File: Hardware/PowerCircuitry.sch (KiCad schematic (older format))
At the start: 25 parts

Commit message: Added master switch etc
I don't like MOSFETs
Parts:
- removed Battery: 3.6V, symbol Device:Battery
- removed Q? (x2): 2N7000, Package_TO_SOT_THT:TO-92_Inline, symbol Transistor_FET:2N7000
- added Battery: Conn_01x02_Male, symbol Connector:Conn_01x02_Male
- added Q? (x2): MMBT3904, Package_TO_SOT_SMD:SOT-23, symbol Transistor_BJT:MMBT3904
- added SW?: SW_Push, symbol Switch:SW_Push
- C2.2: footprint (none) -> Capacitor_SMD:C_0603_1608Metric
- RSense1, RSense2: value 30mOhms -> 30m
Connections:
- wire segments 68 -> 69
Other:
- moved on the sheet: 12VBoostConverter, 3V3Regulator, 6VBoostConverter, C1.1, C1.2, C1.3, C1.4, C2.1, C2.2, C2.3, C2.4, C2.5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

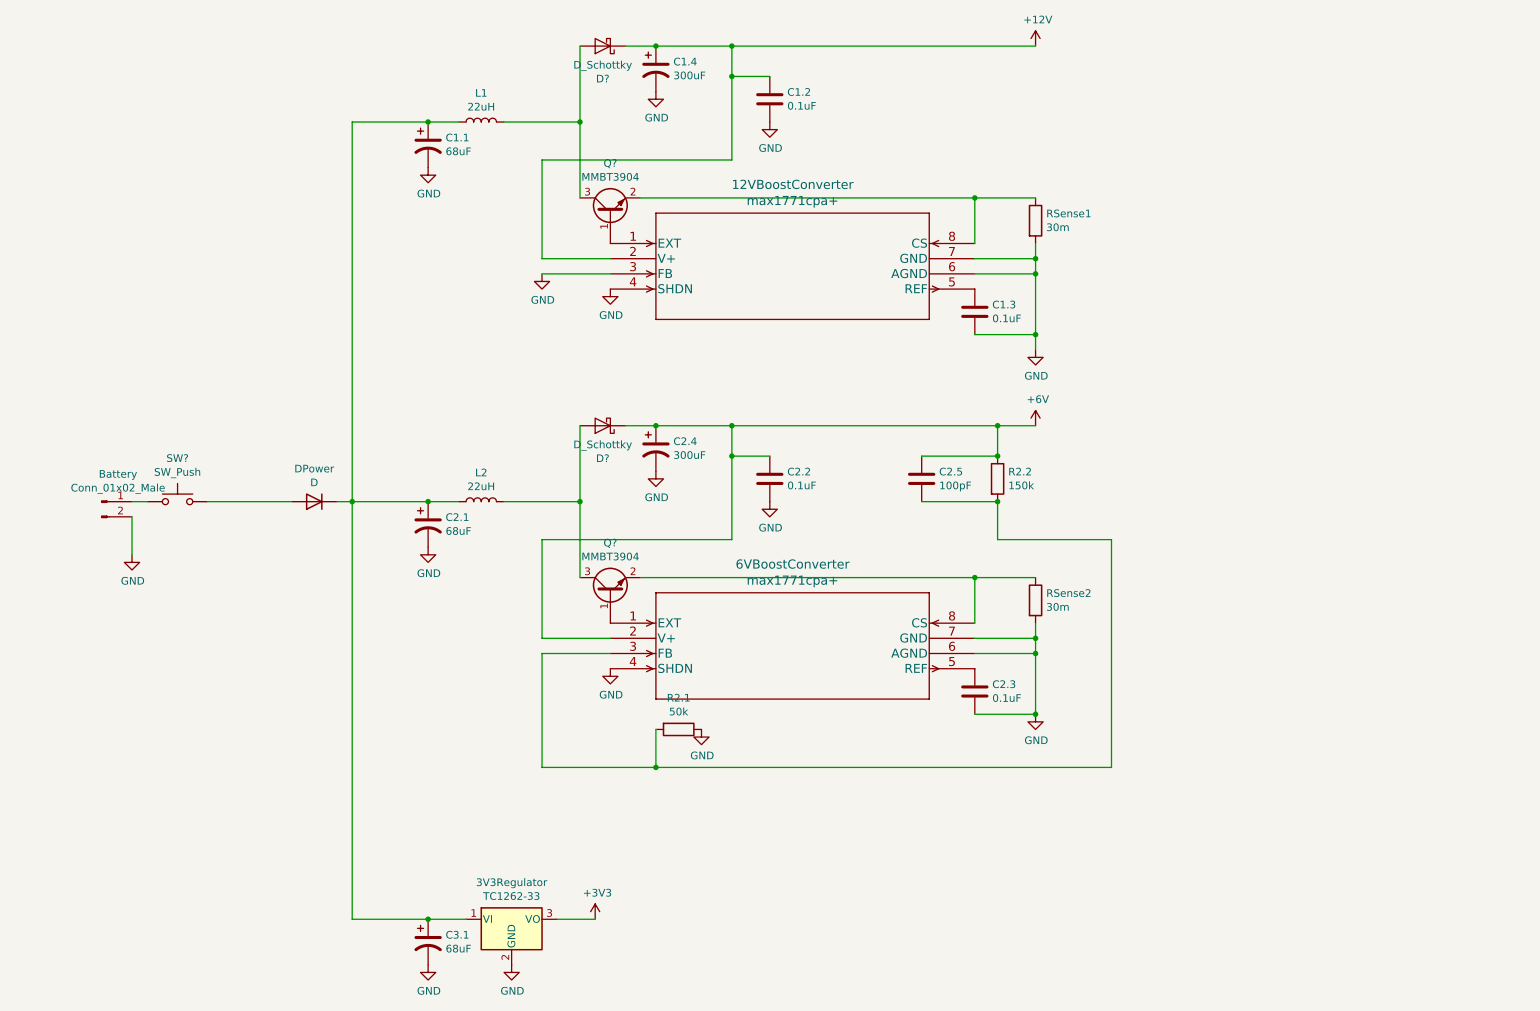
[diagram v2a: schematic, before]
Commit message: Fixed some of the ERC errors
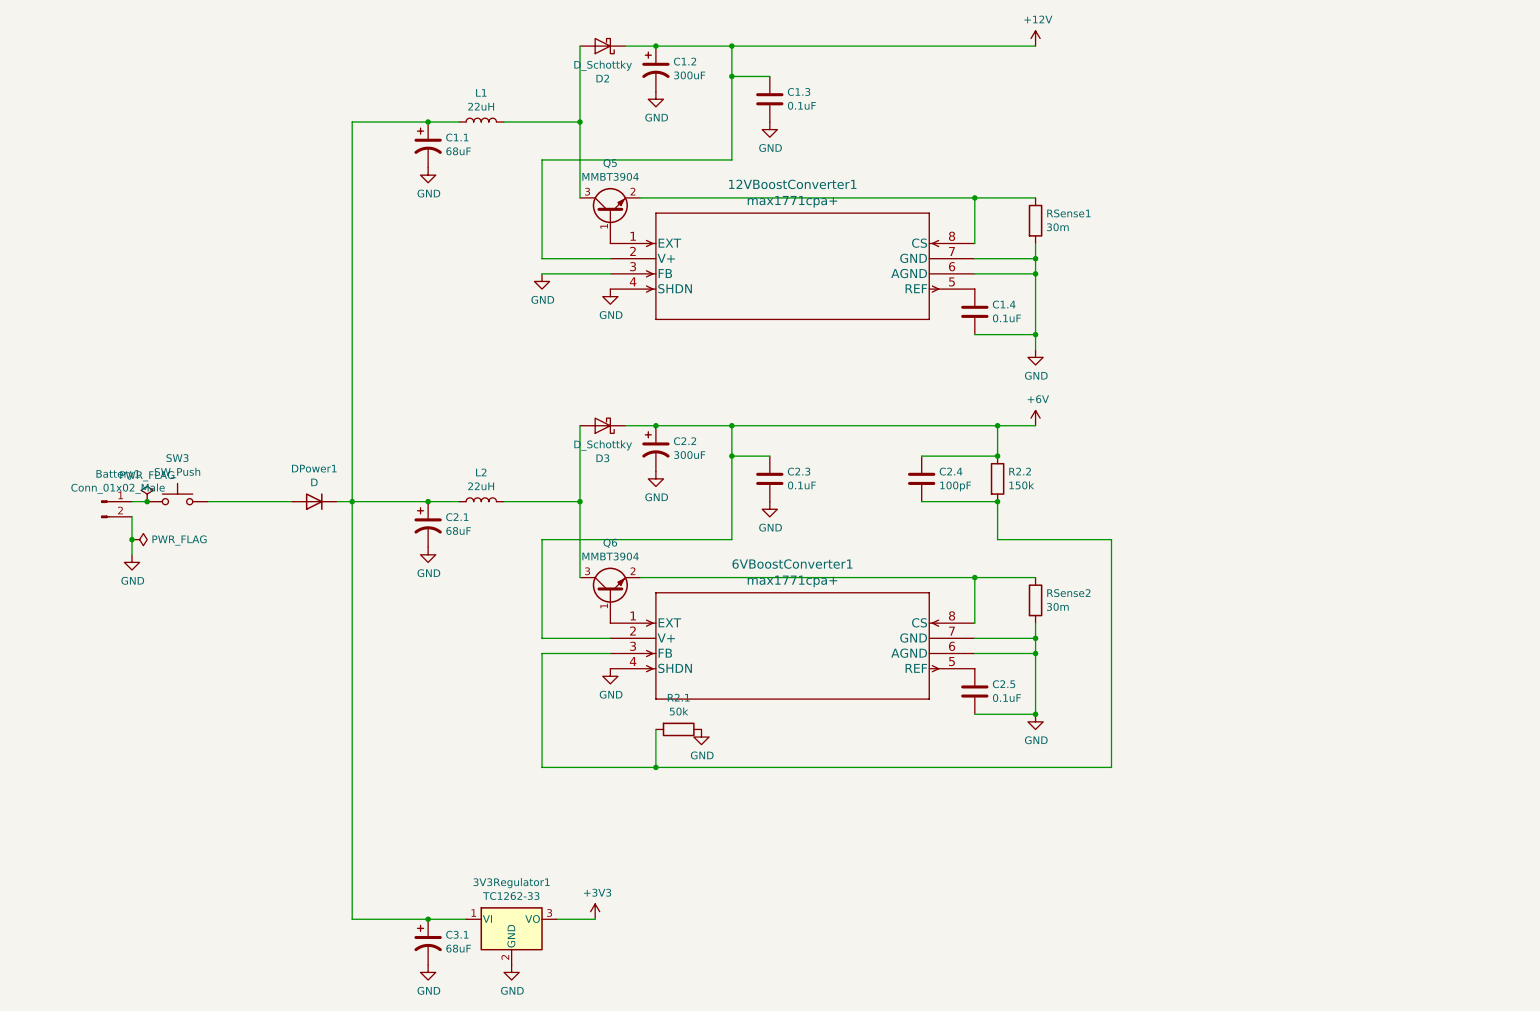
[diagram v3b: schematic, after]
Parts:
- gave numbers to parts that had none: 5
- renumbered 12VBoostConverter to 12VBoostConverter1, 3V3Regulator to 3V3Regulator1, 6VBoostConverter to 6VBoostConverter1, Battery to Battery1, C1.4 to C1.2, C1.2 to C1.3, C1.3 to C1.4, C2.4 to C2.2, C2.2 to C2.3, C2.5 to C2.4, C2.3 to C2.5, DPower to DPower1

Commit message: Created PCB file and laid out components
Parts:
- removed SW3: SW_Push, symbol Switch:SW_Push
- added H1, H2, H3, H4: MountingHole_Pad, MountingHole:MountingHole_3.5mm_Pad_TopBottom, symbol Mechanical:MountingHole_Pad
- added SW3: SW_SPST, Button_Switch_SMD:SW_DIP_SPSTx01_Slide_6.7x4.1mm_W6.73mm_P2.54mm_LowProfile_JPin, symbol Switch:SW_SPST
- 12VBoostConverter1, 6VBoostConverter1: footprint 21-0043D_8_MXM -> footprints:max1771cpa&plus_
- 3V3Regulator1: footprint (none) -> Package_TO_SOT_SMD:SOT-223-3_TabPin2
- Battery1: footprint (none) -> Connector_JST:JST_EH_B2B-EH-A_1x02_P2.50mm_Vertical
- C1.1, C1.2, C1.3, C1.4, C2.1, C2.2, C2.4, C2.5, C3.1: footprint (none) -> Capacitor_SMD:C_0603_1608Metric
- D2, D3, DPower1: footprint (none) -> Diode_SMD:D_0603_1608Metric
- L1, L2: footprint (none) -> Inductor_SMD:L_0603_1608Metric
- R2.1, R2.2, RSense1, RSense2: footprint (none) -> Resistor_SMD:R_0603_1608Metric
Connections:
- net GND: now also H1.1, H2.1, H3.1, H4.1
- net at Battery1.1 (Pin_1): now also SW3.1 (A)
- net at DPower1.2 (A): now also SW3.2 (B)
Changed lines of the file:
@@
 F 0 "3V3Regulator1" H 3500 6742 50  0000 C CNN
 F 1 "TC1262-33" H 3500 6651 50  0000 C CNN
-F 2 "" H 3500 6725 50  0001 C CIN
+F 2 "Package_TO_SOT_SMD:SOT-223-3_TabPin2" H 3500 6725 50  0001 C CIN
 F 3 "http://ww1.microchip.com/downloads/en/DeviceDoc/21373C.pdf" H 3500 6200 50  0001 C CNN
 	1    3500 6500
@@
 F 0 "12VBoostConverter1" H 5350 2437 60  0000 C CNN
 F 1 "max1771cpa+" H 5350 2331 60  0000 C CNN
-F 2 "21-0043D_8_MXM" H 5350 2290 60  0001 C CNN
+F 2 "footprints:max1771cpa&plus_" H 5350 2290 60  0001 C CNN
 F 3 "" H 4150 2050 60  0000 C CNN
 	1    4150 2050
@@
 F 0 "L1" V 3490 1250 50  0000 C CNN
 F 1 "22uH" V 3399 1250 50  0000 C CNN
-F 2 "" H 3300 1250 50  0001 C CNN
+F 2 "Inductor_SMD:L_0603_1608Metric" H 3300 1250 50  0001 C CNN
 F 3 "~" H 3300 1250 50  0001 C CNN
 	1    3300 1250
@@
 F 0 "D2" H 4100 966 50  0000 C CNN
 F 1 "D_Schottky" H 4100 875 50  0000 C CNN
-F 2 "" H 4100 750 50  0001 C CNN
+F 2 "Diode_SMD:D_0603_1608Metric" H 4100 750 50  0001 C CNN
 F 3 "~" H 4100 750 50  0001 C CNN
 	1    4100 750
@@
 F 0 "C1.1" H 3065 1446 50  0000 L CNN
 F 1 "68uF" H 3065 1355 50  0000 L CNN
-F 2 "" H 2950 1400 50  0001 C CNN
+F 2 "Capacitor_SMD:C_0603_1608Metric" H 2950 1400 50  0001 C CNN
 F 3 "~" H 2950 1400 50  0001 C CNN
 	1    2950 1400
@@
 F 0 "C1.2" H 4565 946 50  0000 L CNN
 F 1 "300uF" H 4565 855 50  0000 L CNN
-F 2 "" H 4450 900 50  0001 C CNN
+F 2 "Capacitor_SMD:C_0603_1608Metric" H 4450 900 50  0001 C CNN
 F 3 "~" H 4450 900 50  0001 C CNN
 	1    4450 900
@@
 F 0 "C1.3" H 5315 1146 50  0000 L CNN
 F 1 "0.1uF" H 5315 1055 50  0000 L CNN
-F 2 "" H 5238 950 50  0001 C CNN
+F 2 "Capacitor_SMD:C_0603_1608Metric" H 5238 950 50  0001 C CNN
 F 3 "~" H 5200 1100 50  0001 C CNN
 	1    5200 1100
@@
 F 0 "RSense1" H 7020 1946 50  0000 L CNN
 F 1 "30m" H 7020 1855 50  0000 L CNN
-F 2 "" V 6880 1900 50  0001 C CNN
+F 2 "Resistor_SMD:R_0603_1608Metric" V 6880 1900 50  0001 C CNN
 F 3 "~" H 6950 1900 50  0001 C CNN
 	1    6950 1900
@@
 F 0 "C2.1" H 3065 3946 50  0000 L CNN
 F 1 "68uF" H 3065 3855 50  0000 L CNN
-F 2 "" H 2950 3900 50  0001 C CNN
+F 2 "Capacitor_SMD:C_0603_1608Metric" H 2950 3900 50  0001 C CNN
 F 3 "~" H 2950 3900 50  0001 C CNN
 	1    2950 3900
@@
 F 0 "L2" V 3490 3750 50  0000 C CNN
 F 1 "22uH" V 3399 3750 50  0000 C CNN
-F 2 "" H 3300 3750 50  0001 C CNN
+F 2 "Inductor_SMD:L_0603_1608Metric" H 3300 3750 50  0001 C CNN
 F 3 "~" H 3300 3750 50  0001 C CNN
 	1    3300 3750
@@
 F 0 "D3" H 4100 3466 50  0000 C CNN
 F 1 "D_Schottky" H 4100 3375 50  0000 C CNN
-F 2 "" H 4100 3250 50  0001 C CNN
+F 2 "Diode_SMD:D_0603_1608Metric" H 4100 3250 50  0001 C CNN
 F 3 "~" H 4100 3250 50  0001 C CNN
 	1    4100 3250
@@
 F 0 "C2.2" H 4565 3446 50  0000 L CNN
 F 1 "300uF" H 4565 3355 50  0000 L CNN
-F 2 "" H 4450 3400 50  0001 C CNN
+F 2 "Capacitor_SMD:C_0603_1608Metric" H 4450 3400 50  0001 C CNN
 F 3 "~" H 4450 3400 50  0001 C CNN
 	1    4450 3400
@@
 F 0 "R2.2" H 6770 3646 50  0000 L CNN
 F 1 "150k" H 6770 3555 50  0000 L CNN
-F 2 "" V 6630 3600 50  0001 C CNN
+F 2 "Resistor_SMD:R_0603_1608Metric" V 6630 3600 50  0001 C CNN
 F 3 "~" H 6700 3600 50  0001 C CNN
 	1    6700 3600
@@
 F 0 "C2.4" H 6315 3646 50  0000 L CNN
 F 1 "100pF" H 6315 3555 50  0000 L CNN
-F 2 "" H 6238 3450 50  0001 C CNN
+F 2 "Capacitor_SMD:C_0603_1608Metric" H 6238 3450 50  0001 C CNN
 F 3 "~" H 6200 3600 50  0001 C CNN
 	1    6200 3600
@@
 F 0 "RSense2" H 7020 4446 50  0000 L CNN
 F 1 "30m" H 7020 4355 50  0000 L CNN
-F 2 "" V 6880 4400 50  0001 C CNN
+F 2 "Resistor_SMD:R_0603_1608Metric" V 6880 4400 50  0001 C CNN
 F 3 "~" H 6950 4400 50  0001 C CNN
 	1    6950 4400
@@
 F 0 "R2.1" V 4393 5250 50  0000 C CNN
 F 1 "50k" V 4484 5250 50  0000 C CNN
-F 2 "" V 4530 5250 50  0001 C CNN
+F 2 "Resistor_SMD:R_0603_1608Metric" V 4530 5250 50  0001 C CNN
 F 3 "~" H 4600 5250 50  0001 C CNN
 	1    4600 5250
@@
 F 0 "C1.4" H 6665 2546 50  0000 L CNN
 F 1 "0.1uF" H 6665 2455 50  0000 L CNN
-F 2 "" H 6588 2350 50  0001 C CNN
+F 2 "Capacitor_SMD:C_0603_1608Metric" H 6588 2350 50  0001 C CNN
 F 3 "~" H 6550 2500 50  0001 C CNN
 	1    6550 2500
@@
 F 0 "C2.5" H 6665 5046 50  0000 L CNN
 F 1 "0.1uF" H 6665 4955 50  0000 L CNN
-F 2 "" H 6588 4850 50  0001 C CNN
+F 2 "Capacitor_SMD:C_0603_1608Metric" H 6588 4850 50  0001 C CNN
 F 3 "~" H 6550 5000 50  0001 C CNN
 	1    6550 5000
@@
 F 0 "C3.1" H 3065 6696 50  0000 L CNN
 F 1 "68uF" H 3065 6605 50  0000 L CNN
-F 2 "" H 2950 6650 50  0001 C CNN
+F 2 "Capacitor_SMD:C_0603_1608Metric" H 2950 6650 50  0001 C CNN
 F 3 "~" H 2950 6650 50  0001 C CNN
 	1    2950 6650
@@
 Connection ~ 2950 6500
 $Comp
-L Switch:SW_Push SW3
-U 1 1 607B163F
-P 1300 3750
-F 0 "SW3" H 1300 4035 50  0000 C CNN
-F 1 "SW_Push" H 1300 3944 50  0000 C CNN
-F 2 "" H 1300 3950 50  0001 C CNN
-F 3 "~" H 1300 3950 50  0001 C CNN
-	1    1300 3750
-	1    0    0    -1
-$EndComp
-$Comp
 L Device:D DPower1
 U 1 1 607B8542
@@
 F 0 "DPower1" H 2200 3534 50  0000 C CNN
 F 1 "D" H 2200 3625 50  0000 C CNN
-F 2 "" H 2200 3750 50  0001 C CNN
+F 2 "Diode_SMD:D_0603_1608Metric" H 2200 3750 50  0001 C CNN
 F 3 "~" H 2200 3750 50  0001 C CNN
 	1    2200 3750
@@
 F 0 "Battery1" H 908 3931 50  0000 C CNN
 F 1 "Conn_01x02_Male" H 908 3840 50  0000 C CNN
-F 2 "" H 800 3750 50  0001 C CNN
+F 2 "Connector_JST:JST_EH_B2B-EH-A_1x02_P2.50mm_Vertical" H 800 3750 50  0001 C CNN
 F 3 "~" H 800 3750 50  0001 C CNN
 	1    800  3750
@@
 F 0 "6VBoostConverter1" H 5350 4937 60  0000 C CNN
 F 1 "max1771cpa+" H 5350 4831 60  0000 C CNN
-F 2 "21-0043D_8_MXM" H 5350 4790 60  0001 C CNN
+F 2 "footprints:max1771cpa&plus_" H 5350 4790 60  0001 C CNN
 F 3 "" H 4150 4550 60  0000 C CNN
 	1    4150 4550
@@
 Wire Wire Line
 	1500 3750 2050 3750
+Wire Wire Line
+	2450 1250 2450 3750
+$Comp
+L Switch:SW_SPST SW3
+U 1 1 608DCB23
+P 1300 3750
+F 0 "SW3" H 1300 3985 50  0000 C CNN
+F 1 "SW_SPST" H 1300 3894 50  0000 C CNN
+F 2 "Button_Switch_SMD:SW_DIP_SPSTx01_Slide_6.7x4.1mm_W6.73mm_P2.54mm_LowProfile_JPin" H 1300 3750 50  0001 C CNN
+F 3 "~" H 1300 3750 50  0001 C CNN
+	1    1300 3750
+	1    0    0    -1
+$EndComp
 Connection ~ 1100 3750
-Wire Wire Line
-	2450 1250 2450 3750
+$Comp
+L Mechanical:MountingHole_Pad H1
+U 1 1 6090A199
+P 9100 1450
+F 0 "H1" V 9054 1600 50  0000 L CNN
+F 1 "MountingHole_Pad" V 9145 1600 50  0000 L CNN
+F 2 "MountingHole:MountingHole_3.5mm_Pad_TopBottom" H 9100 1450 50  0001 C CNN
+F 3 "~" H 9100 1450 50  0001 C CNN
+	1    9100 1450
+	0    1    1    0
+$EndComp
+$Comp
+L Mechanical:MountingHole_Pad H2
+U 1 1 6090BABB
+P 9100 1650
+F 0 "H2" V 9054 1800 50  0000 L CNN
+F 1 "MountingHole_Pad" V 9145 1800 50  0000 L CNN
+F 2 "MountingHole:MountingHole_3.5mm_Pad_TopBottom" H 9100 1650 50  0001 C CNN
+F 3 "~" H 9100 1650 50  0001 C CNN
+	1    9100 1650
+	0    1    1    0
+$EndComp
+$Comp
+L Mechanical:MountingHole_Pad H3
+U 1 1 6090BF65
+P 9100 1850
+F 0 "H3" V 9054 2000 50  0000 L CNN
+F 1 "MountingHole_Pad" V 9145 2000 50  0000 L CNN
+F 2 "MountingHole:MountingHole_3.5mm_Pad_TopBottom" H 9100 1850 50  0001 C CNN
+F 3 "~" H 9100 1850 50  0001 C CNN
+	1    9100 1850
+	0    1    1    0
+$EndComp
+$Comp
+L Mechanical:MountingHole_Pad H4
+U 1 1 6090BF6B
+P 9100 2050
+F 0 "H4" V 9054 2200 50  0000 L CNN
+F 1 "MountingHole_Pad" V 9145 2200 50  0000 L CNN
+F 2 "MountingHole:MountingHole_3.5mm_Pad_TopBottom" H 9100 2050 50  0001 C CNN
+F 3 "~" H 9100 2050 50  0001 C CNN
+	1    9100 2050
+	0    1    1    0
+$EndComp
+Wire Wire Line
+	9000 1450 9000 1650
+Connection ~ 9000 1650
+Wire Wire Line
+	9000 1650 9000 1750
+Connection ~ 9000 1850
+Wire Wire Line
+	9000 1850 9000 2050
+$Comp
+L power:GND #PWR053
+U 1 1 6090F428
+P 9000 1750
+F 0 "#PWR053" H 9000 1500 50  0001 C CNN
+F 1 "GND" V 9005 1622 50  0000 R CNN
+F 2 "" H 9000 1750 50  0001 C CNN
+F 3 "" H 9000 1750 50  0001 C CNN
+	1    9000 1750
+	0    1    1    0
+$EndComp
+Connection ~ 9000 1750
+Wire Wire Line
+	9000 1750 9000 1850
 $EndSCHEMATC

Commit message: Final changes for this first draft
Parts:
- added J4, J5: Conn_01x02_Male, Connector_PinHeader_2.54mm:PinHeader_2x01_P2.54mm_Vertical, symbol Connector:Conn_01x02_Male
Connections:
- net +12V: now also J4.2 (Pin_2)
- net +6V: now also J5.2 (Pin_2)
- net GND: now also J4.1 (Pin_1), J5.1 (Pin_1)
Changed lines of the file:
@@
 Wire Wire Line
 	9000 1750 9000 1850
+$Comp
+L Connector:Conn_01x02_Male J4
+U 1 1 609DE2A3
+P 9400 3000
+F 0 "J4" H 9372 2882 50  0000 R CNN
+F 1 "Conn_01x02_Male" H 9372 2973 50  0000 R CNN
+F 2 "Connector_PinHeader_2.54mm:PinHeader_2x01_P2.54mm_Vertical" H 9400 3000 50  0001 C CNN
+F 3 "~" H 9400 3000 50  0001 C CNN
+	1    9400 3000
+	-1   0    0    1
+$EndComp
+Wire Wire Line
+	9200 2900 9100 2900
+Wire Wire Line
+	9200 3000 9100 3000
+Wire Wire Line
+	9100 3000 9100 3100
+Wire Wire Line
+	9100 2900 9100 2800
+$Comp
+L power:+12V #PWR054
+U 1 1 609E333D
+P 9100 2800
+F 0 "#PWR054" H 9100 2650 50  0001 C CNN
+F 1 "+12V" H 9115 2973 50  0000 C CNN
+F 2 "" H 9100 2800 50  0001 C CNN
+F 3 "" H 9100 2800 50  0001 C CNN
+	1    9100 2800
+	1    0    0    -1
+$EndComp
+$Comp
+L power:GND #PWR055
+U 1 1 609E5451
+P 9100 3100
+F 0 "#PWR055" H 9100 2850 50  0001 C CNN
+F 1 "GND" H 9105 2927 50  0000 C CNN
+F 2 "" H 9100 3100 50  0001 C CNN
+F 3 "" H 9100 3100 50  0001 C CNN
+	1    9100 3100
+	1    0    0    -1
+$EndComp
+$Comp
+L Connector:Conn_01x02_Male J5
+U 1 1 609E8D04
+P 9400 3850
+F 0 "J5" H 9372 3732 50  0000 R CNN
+F 1 "Conn_01x02_Male" H 9372 3823 50  0000 R CNN
+F 2 "Connector_PinHeader_2.54mm:PinHeader_2x01_P2.54mm_Vertical" H 9400 3850 50  0001 C CNN
+F 3 "~" H 9400 3850 50  0001 C CNN
+	1    9400 3850
+	-1   0    0    1
+$EndComp
+Wire Wire Line
+	9200 3750 9100 3750
+Wire Wire Line
+	9200 3850 9100 3850
+Wire Wire Line
+	9100 3850 9100 3950
+Wire Wire Line
+	9100 3750 9100 3650
+$Comp
+L power:GND #PWR057
+U 1 1 609E8D14
+P 9100 3950
+F 0 "#PWR057" H 9100 3700 50  0001 C CNN
+F 1 "GND" H 9105 3777 50  0000 C CNN
+F 2 "" H 9100 3950 50  0001 C CNN
+F 3 "" H 9100 3950 50  0001 C CNN
+	1    9100 3950
+	1    0    0    -1
+$EndComp
+$Comp
+L power:+6V #PWR056
+U 1 1 609EA9AA
+P 9100 3650
+F 0 "#PWR056" H 9100 3500 50  0001 C CNN
+F 1 "+6V" H 9115 3823 50  0000 C CNN
+F 2 "" H 9100 3650 50  0001 C CNN
+F 3 "" H 9100 3650 50  0001 C CNN
+	1    9100 3650
+	1    0    0    -1
+$EndComp
 $EndSCHEMATC
